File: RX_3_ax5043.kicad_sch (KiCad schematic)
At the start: 19 parts, among them P3 CONUFL001-SMD-T, Q5 DMP2160UWQ-7, U17 AX5043

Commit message: Add licensing
Use CERN-OHL-W version 2

Signed-off-by: Corey Minyard <corey@minyard.net>
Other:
- note removed: "RECEIVER 3"
- title: Radiation Tolerant PacSat Communication -> AX5043 Receiver 3
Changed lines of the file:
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@@
 	(paper "USLedger")
 	(title_block
-		(title "Radiation Tolerant PacSat Communication")
-		(date "2023-06-17")
-		(rev "A")
+		(title "AX5043 Receiver 3")
+		(date "2026-08-20")
+		(rev "4.0")
 		(company "AMSAT-NA")
-		(comment 1 "N5BRG")
-	)
-	(text "RECEIVER 3"
-		(exclude_from_sim no)
-		(at 339.09 247.65 0)
-		(effects
-			(font
-				(size 6.096 6.096)
-			)
-			(justify left bottom)
-		)
+		(comment 1 "AE5KM")
+		(comment 2 "Copyright Corey Minyard, 2026")
+		(comment 3 "Licensed under CERN-OHL-W version 2")
 	)
 	(text "RX3+"

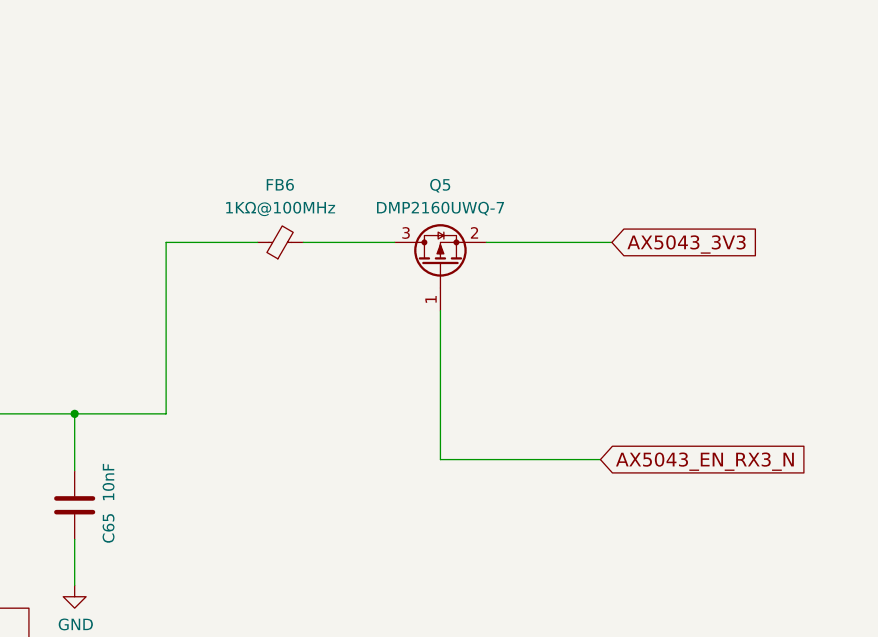
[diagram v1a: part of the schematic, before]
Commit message: Cost reduce the AX5043 power control
Change the MOSFET + ferrite bead combo on all the AX5043 power inputs
to a inrush-controlled power controller.  The space-rated ferrites are
just too expensive.

Signed-off-by: Corey Minyard <corey@minyard.net>
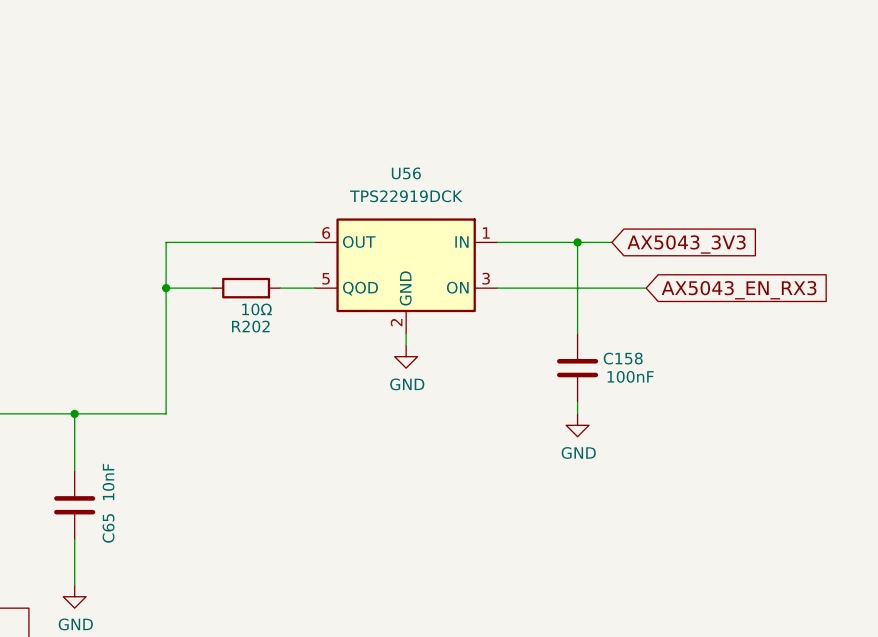
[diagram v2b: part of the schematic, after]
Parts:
- removed FB6: 1KΩ@100MHz, Inductor_SMD:L_0603_1608Metric_Pad1.05x0.95mm_HandSolder, symbol Device:FerriteBead_Small
- removed Q5: DMP2160UWQ-7, Package_TO_SOT_SMD:SOT-323_SC-70, symbol Transistor_FET:Q_PMOS_GSD
- added C158: 100nF, Capacitor_SMD:C_0402_1005Metric_Pad0.74x0.62mm_HandSolder, symbol Device:C
- added R202: 10Ω, Resistor_SMD:R_0402_1005Metric_Pad0.72x0.64mm_HandSolder, symbol Device:R
- added U56: TPS22919DCK, Package_TO_SOT_SMD:SOT-363_SC-70-6, symbol Power_Management:TPS22919DCK
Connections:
- net AX5043_3V3: now also C158.1, U56.1 (IN)
- net GND: now also C158.2, U56.2 (GND)
- net at C65.1, U17.23 (VDD_IO): now also R202.1, U56.6 (OUT)
- new net: R202.2, U56.5 (QOD)
- new net AX5043_EN_RX3: U56.3 (ON)

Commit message: Fix clearance around differential pairs
Meet the 5X requirement for trace width vs clearance.

Signed-off-by: Corey Minyard <corey@minyard.net>
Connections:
- net RX3_N renamed RX3ANT_N
- net RX3_P renamed RX3ANT_P
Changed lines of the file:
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@@
 		)
 	)
-	(label "RX3_N"
+	(label "RX3ANT_N"
 		(at 228.6 124.46 0)
 		(effects
@@
 		)
 	)
-	(label "RX3_P"
+	(label "RX3ANT_P"
 		(at 228.6 121.92 0)
 		(effects

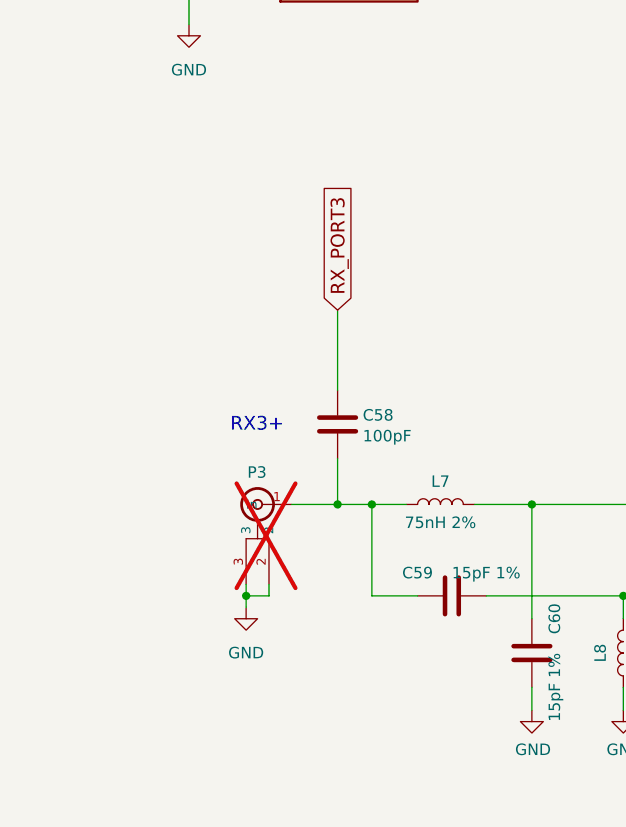
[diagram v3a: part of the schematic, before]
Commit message: Remove U.FL connectors from all AX5043 RX connections except AX5043 4
They aren't necessary.  If you need to pull off an RX line for another
board, you can use 4, and you can use 4 for testing.

Signed-off-by: Corey Minyard <corey@minyard.net>
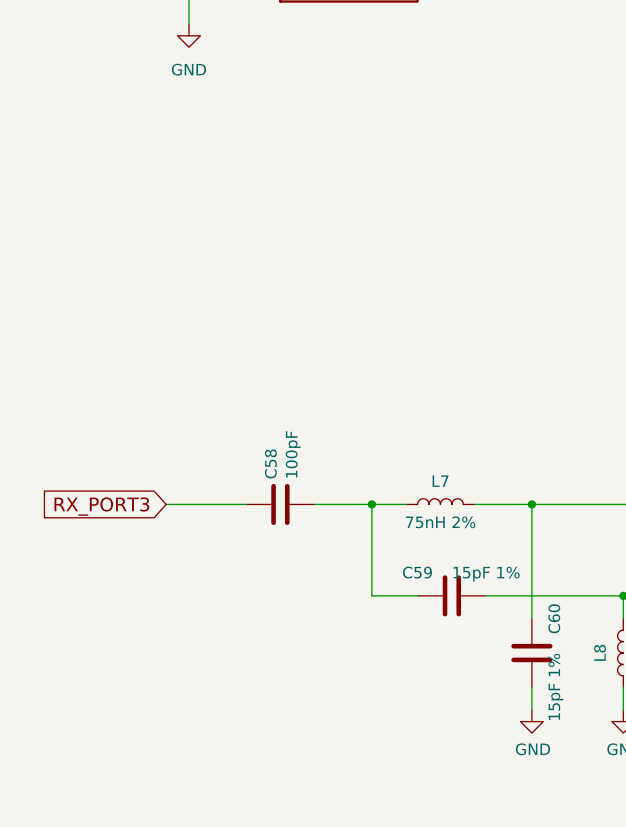
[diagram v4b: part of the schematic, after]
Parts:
- removed P3: CONUFL001-SMD-T, PacSatDev_misc:CONN1_CONUFL_TEC, symbol PACSAT_DEV_misc:U_FL
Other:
- note removed: "RX3+"
- moved on the sheet: C58
